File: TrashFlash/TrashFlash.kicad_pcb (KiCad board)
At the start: 2 copper layers, 96 parts, among them IC1 LTC3643IUDD#PBF, IC10 BQ24230RGTR, IC2 ADG5419BCPZ-RL7, IC3 BQ27426YZFR, IC4 SN74LXC2T45QDTTRQ1, IC5 TPS63900DSKR, IC6 TPS63900DSKR, IC7 LP5024RSMR, IC8 AD8615AUJZ-REEL, IC9 BQ29732DSER, J1 USB4800-03-A, Q1 BC56-10PA,115, Q2 BC56-10PA,115, Q3 BC56-10PA,115, Q4 BC56-10PA,115, Q5 PMDPB30XNAX, U1 SI5448DU-T1-GE3, U2 SI5448DU-T1-GE3

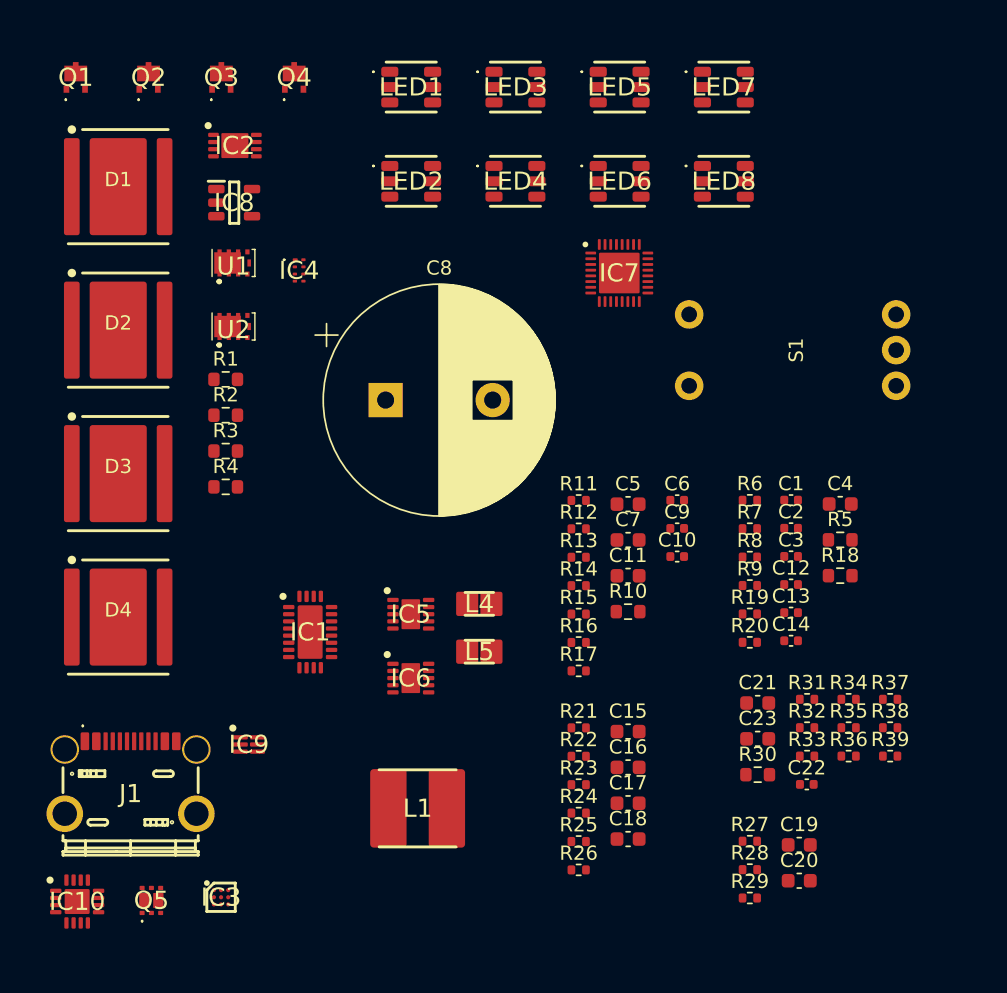
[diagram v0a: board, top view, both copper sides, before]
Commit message: Footprints 3D model fixed
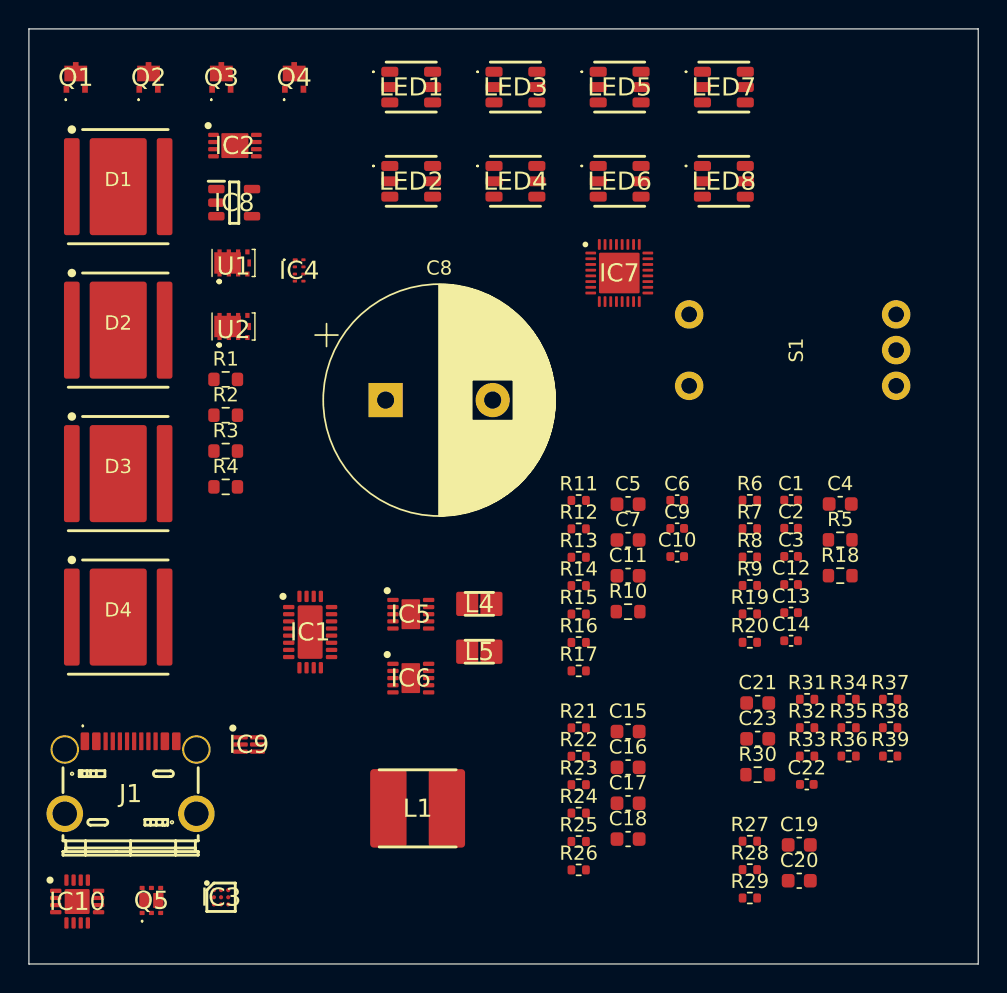
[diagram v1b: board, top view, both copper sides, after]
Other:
- board outline added: 66.5 x 65.5 mm
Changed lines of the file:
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@@
 		)
 		(embedded_fonts no)
-		(model "150353M153300.stp"
+		(model "${KIPRJMOD}/TrashFlash.pretty/3D/150353M153300.stp"
 			(offset
 				(xyz 0 0 0)
@@
 			)
 			(rotate
-				(xyz 0 0 0)
+				(xyz -0 -0 -180)
 			)
 		)
@@
 		)
 		(embedded_fonts no)
-		(model "LP5024RSMR.stp"
+		(model "${KIPRJMOD}/TrashFlash.pretty/3D/LP5024RSMR.stp"
 			(offset
 				(xyz 0 0 0)
@@
 		)
 		(embedded_fonts no)
-		(model "ADG5419BCPZ-RL7.stp"
+		(model "${KIPRJMOD}/TrashFlash.pretty/3D/ADG5419BCPZ-RL7.stp"
 			(offset
 				(xyz 0 0 0)
@@
 		)
 		(embedded_fonts no)
-		(model "PMDPB30XNAX.stp"
+		(model "${KIPRJMOD}/TrashFlash.pretty/3D/PMDPB30XNAX.stp"
 			(offset
-				(xyz 0 0 0.03999999851)
+				(xyz 0 0 0)
 			)
 			(scale
@@
 			)
 			(rotate
-				(xyz 90 -180 0)
+				(xyz 0 0 0)
 			)
 		)
@@
 		)
 		(embedded_fonts no)
-		(model "TPS63900DSKR.stp"
+		(model "${KIPRJMOD}/TrashFlash.pretty/3D/TPS63900DSKR.stp"
 			(offset
 				(xyz 0 0 0)
@@
 		)
 		(embedded_fonts no)
-		(model "${KIPRJMOD}/TrashFlash.pretty/ec11e09244aq.step"
+		(model "${KIPRJMOD}/TrashFlash.pretty/3D/ec11e09244aq.step"
 			(offset
 				(xyz 2.5 7.5 3.5)
@@
 		)
 		(embedded_fonts no)
-		(model "150353M153300.stp"
+		(model "${KIPRJMOD}/TrashFlash.pretty/3D/150353M153300.stp"
 			(offset
 				(xyz 0 0 0)
@@
 			)
 			(rotate
-				(xyz 0 0 0)
+				(xyz -0 -0 -180)
 			)
 		)
@@
 		)
 		(embedded_fonts no)
-		(model "SN74LXC2T45QDTTRQ1.stp"
+		(model "${KIPRJMOD}/TrashFlash.pretty/3D/SN74LXC2T45QDTTRQ1.stp"
 			(offset
 				(xyz 0 0 0)
@@
 			)
 			(rotate
-				(xyz 0 0 0)
+				(xyz -0 -0 -0)
 			)
 		)
@@
 		)
 		(embedded_fonts no)
-		(model "150353M153300.stp"
+		(model "${KIPRJMOD}/TrashFlash.pretty/3D/150353M153300.stp"
 			(offset
 				(xyz 0 0 0)
@@
 			)
 			(rotate
-				(xyz 0 0 0)
+				(xyz -0 -0 -180)
 			)
 		)
@@
 		)
 		(embedded_fonts no)
-		(model "BC56-10PA,115.stp"
+		(model "${KIPRJMOD}/TrashFlash.pretty/3D/BC56-10PA,115.stp"
 			(offset
-				(xyz 0.8600000014 1.509999968 1.129999978)
+				(xyz 0.85 1.55 1.1)
 			)
 			(scale
@@
 			)
 			(rotate
-				(xyz 90 0 -180)
+				(xyz 90 -0 -180)
 			)
 		)
@@
 			)
 		)
+		(model "${KIPRJMOD}/TrashFlash.pretty/3D/SI5448DU-T1-GE3.stp"
+			(offset
+				(xyz 0 0 0)
+			)
+			(scale
+				(xyz 1 1 1)
+			)
+			(rotate
+				(xyz -90 -0 -0)
+			)
+		)
 	)
 	(footprint "TrashFlash:XFL05K"
@@
 		)
 		(embedded_fonts no)
-		(model "TPS63900DSKR.stp"
+		(model "${KIPRJMOD}/TrashFlash.pretty/3D/TPS63900DSKR.stp"
 			(offset
 				(xyz 0 0 0)
@@
 		)
 		(embedded_fonts no)
-		(model "AD8615AUJZ-REEL.stp"
+		(model "${KIPRJMOD}/TrashFlash.pretty/3D/AD8615AUJZ-REEL.stp"
 			(offset
 				(xyz 0 0 0)
@@
 		)
 		(embedded_fonts no)
-		(model "BQ24230RGTR.stp"
+		(model "${KIPRJMOD}/TrashFlash.pretty/3D/BQ24230RGTR.stp"
 			(offset
 				(xyz 0 0 0)
@@
 		)
 		(embedded_fonts no)
-		(model "150353M153300.stp"
+		(model "${KIPRJMOD}/TrashFlash.pretty/3D/150353M153300.stp"
 			(offset
 				(xyz 0 0 0)
@@
 			)
 			(rotate
-				(xyz 0 0 0)
+				(xyz -0 -0 -180)
 			)
 		)
@@
 			)
 		)
+		(model "${KIPRJMOD}/TrashFlash.pretty/3D/SI5448DU-T1-GE3.stp"
+			(offset
+				(xyz 0 0 0)
+			)
+			(scale
+				(xyz 1 1 1)
+			)
+			(rotate
+				(xyz -90 -0 -0)
+			)
+		)
 	)
 	(footprint "Resistor_SMD:R_0402_1005Metric"
@@
 		)
 		(embedded_fonts no)
+		(model "${KIPRJMOD}/TrashFlash.pretty/3D/USB4800-03-A.stp"
+			(offset
+				(xyz 0 -4.25 0)
+			)
+			(scale
+				(xyz 1 1 1)
+			)
+			(rotate
+				(xyz -90 -0 -0)
+			)
+		)
 	)
 	(footprint "Resistor_SMD:R_0402_1005Metric"
@@
 		)
 		(embedded_fonts no)
-		(model "74438343022.stp"
+		(model "${KIPRJMOD}/TrashFlash.pretty/3D/74438343022.stp"
 			(offset
 				(xyz 0 0 0)
@@
 		)
 		(embedded_fonts no)
-		(model "LTC3643IUDD#PBF.stp"
+		(model "${KIPRJMOD}/TrashFlash.pretty/3D/LTC3643IUDD#PBF.stp"
 			(offset
 				(xyz 0 0 0)
@@
 		)
 		(embedded_fonts no)
-		(model "150353M153300.stp"
+		(model "${KIPRJMOD}/TrashFlash.pretty/3D/150353M153300.stp"
 			(offset
 				(xyz 0 0 0)
@@
 			)
 			(rotate
-				(xyz 0 0 0)
+				(xyz -0 -0 -180)
 			)
 		)
@@
 		)
 		(embedded_fonts no)
-		(model "BQ29732DSER.stp"
+		(model "${KIPRJMOD}/TrashFlash.pretty/3D/BQ29732DSER.stp"
 			(offset
-				(xyz 0 0 0.02999999888)
+				(xyz 0 0 0)
 			)
 			(scale
@@
 			)
 			(rotate
-				(xyz -90 0 -90)
+				(xyz -90 -0 -90)
 			)
 		)
@@
 		)
 		(embedded_fonts no)
-		(model "BQ27426YZFR.stp"
+		(model "${KIPRJMOD}/TrashFlash.pretty/3D/BQ27426YZFR.stp"
 			(offset
 				(xyz 0 0 0)
@@
 		)
 		(embedded_fonts no)
-		(model "74438367068.stp"
+		(model "${KIPRJMOD}/TrashFlash.pretty/3D/74438367068.stp"
 			(offset
 				(xyz 0 0 0)
@@
 		)
 		(embedded_fonts no)
-		(model "150353M153300.stp"
+		(model "${KIPRJMOD}/TrashFlash.pretty/3D/150353M153300.stp"
 			(offset
 				(xyz 0 0 0)
@@
 			)
 			(rotate
-				(xyz 0 0 0)
+				(xyz -0 -0 -180)
 			)
 		)
@@
 		)
 		(embedded_fonts no)
-		(model "BC56-10PA,115.stp"
+		(model "${KIPRJMOD}/TrashFlash.pretty/3D/BC56-10PA,115.stp"
 			(offset
-				(xyz 0.8600000014 1.509999968 1.129999978)
+				(xyz 0.85 1.55 1.1)
 			)
 			(scale
@@
 			)
 			(rotate
-				(xyz 90 0 -180)
+				(xyz 90 -0 -180)
 			)
 		)
@@
 		)
 		(embedded_fonts no)
-		(model "BC56-10PA,115.stp"
+		(model "${KIPRJMOD}/TrashFlash.pretty/3D/BC56-10PA,115.stp"
 			(offset
-				(xyz 0.8600000014 1.509999968 1.129999978)
+				(xyz 0.85 1.55 1.1)
 			)
 			(scale
@@
 			)
 			(rotate
-				(xyz 90 0 -180)
+				(xyz 90 -0 -180)
 			)
 		)
@@
 		)
 		(embedded_fonts no)
-		(model "74438343022.stp"
+		(model "${KIPRJMOD}/TrashFlash.pretty/3D/74438343022.stp"
 			(offset
 				(xyz 0 0 0)
@@
 		)
 		(embedded_fonts no)
-		(model "150353M153300.stp"
+		(model "${KIPRJMOD}/TrashFlash.pretty/3D/150353M153300.stp"
 			(offset
 				(xyz 0 0 0)
@@
 			)
 			(rotate
-				(xyz 0 0 0)
+				(xyz -0 -0 -180)
 			)
 		)
@@
 		)
 		(embedded_fonts no)
-		(model "150353M153300.stp"
+		(model "${KIPRJMOD}/TrashFlash.pretty/3D/150353M153300.stp"
 			(offset
 				(xyz 0 0 0)
@@
 			)
 			(rotate
-				(xyz 0 0 0)
+				(xyz -0 -0 -180)
 			)
 		)
@@
 		)
 		(embedded_fonts no)
-		(model "BC56-10PA,115.stp"
+		(model "${KIPRJMOD}/TrashFlash.pretty/3D/BC56-10PA,115.stp"
 			(offset
-				(xyz 0.8600000014 1.509999968 1.129999978)
+				(xyz 0.85 1.55 1.1)
 			)
 			(scale
@@
 			)
 			(rotate
-				(xyz 90 0 -180)
+				(xyz 90 -0 -180)
 			)
 		)
 	)
+	(gr_rect
+		(start 84 71)
+		(end 150.5 136.5)
+		(stroke
+			(width 0.05)
+			(type default)
+		)
+		(fill no)
+		(layer "Edge.Cuts")
+	)
 	(embedded_fonts no)

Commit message: 3d models and footprints
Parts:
- moved C8 50.0 mm to (156.5, 112.5)

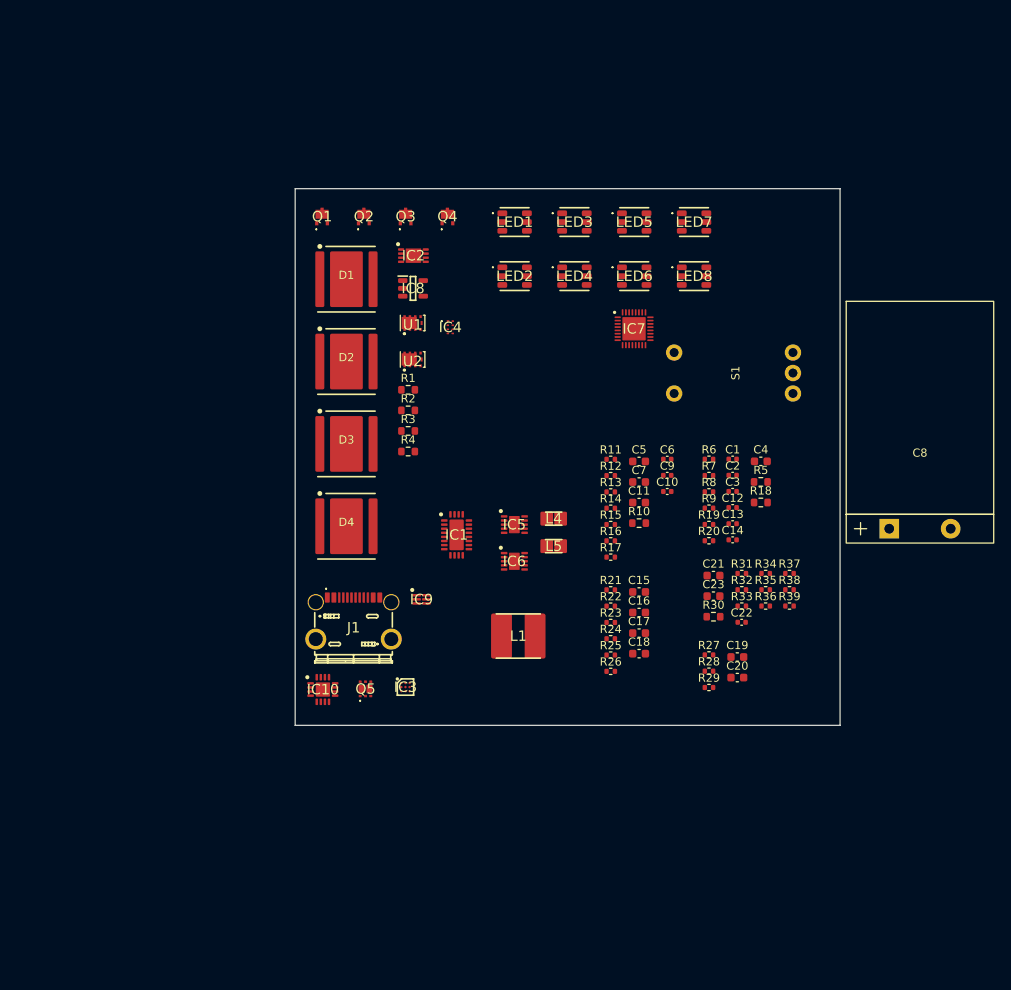
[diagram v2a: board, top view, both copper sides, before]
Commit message: Added 3D-models to footprints, PCB outline and component placement
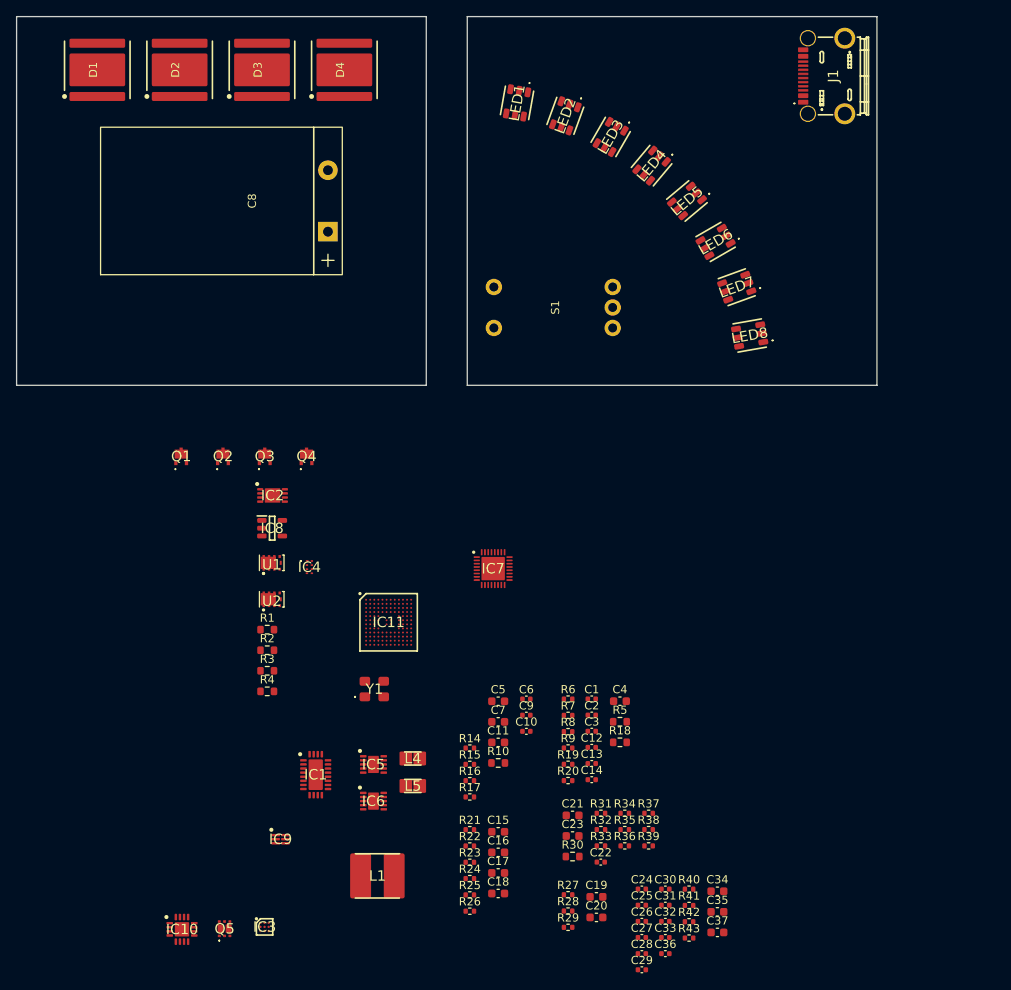
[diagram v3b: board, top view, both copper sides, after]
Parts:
- removed R11: 100k, Resistor_SMD:R_0402_1005Metric
- removed R12: 33k, Resistor_SMD:R_0402_1005Metric
- removed R13: 27k, Resistor_SMD:R_0402_1005Metric
- added C24: 6.8p, Capacitor_SMD:C_0402_1005Metric, F.Cu at (126.3, 156.5)
- added C25: 6.8p, Capacitor_SMD:C_0402_1005Metric, F.Cu at (126.3, 158.4)
- added C26: 100n, Capacitor_SMD:C_0402_1005Metric, F.Cu at (126.3, 160.4)
- added C27: 100n, Capacitor_SMD:C_0402_1005Metric, F.Cu at (126.3, 162.4)
- added C28: 100n, Capacitor_SMD:C_0402_1005Metric, F.Cu at (126.3, 164.4)
- added C29: 100n, Capacitor_SMD:C_0402_1005Metric, F.Cu at (126.3, 166.3)
- added C30: 100n, Capacitor_SMD:C_0402_1005Metric, F.Cu at (129.2, 156.5)
- added C31: 100n, Capacitor_SMD:C_0402_1005Metric, F.Cu at (129.2, 158.4)
- added C32: 100n, Capacitor_SMD:C_0402_1005Metric, F.Cu at (129.2, 160.4)
- added C33: 100n, Capacitor_SMD:C_0402_1005Metric, F.Cu at (129.2, 162.4)
- added C34: 4.7u, Capacitor_SMD:C_0603_1608Metric, F.Cu at (135.5, 156.8)
- added C35: 1u, Capacitor_SMD:C_0603_1608Metric, F.Cu at (135.5, 159.3)
- added C36: 10n, Capacitor_SMD:C_0402_1005Metric, F.Cu at (129.2, 164.4)
- added C37: 1u, Capacitor_SMD:C_0603_1608Metric, F.Cu at (135.5, 161.8)
- added IC11: STM32L471QEI6, TrashFlash:BGA132C50P12X12_700X700X60, F.Cu at (95.4, 123.9)
- added R40: 1k, Resistor_SMD:R_0402_1005Metric, F.Cu at (132.1, 156.5)
- added R41: 1k, Resistor_SMD:R_0402_1005Metric, F.Cu at (132.1, 158.5)
- added R42: 1k, Resistor_SMD:R_0402_1005Metric, F.Cu at (132.1, 160.5)
- added R43: 1k, Resistor_SMD:R_0402_1005Metric, F.Cu at (132.1, 162.5)
- added Y1: ECS-160-8-33B2-CTN-TR3, TrashFlash:ECS160833B2CTNTR3, F.Cu at (93.7, 132.1)
- moved J1 89.2 mm to (149.7, 57.2), turned to 90 degrees
- moved C8 77.5 mm to (88.0, 76.2), turned to 90 degrees
- moved D4 55.7 mm to (90.0, 56.5), turned to 90 degrees
- moved D3 46.8 mm to (80.0, 56.5), turned to 90 degrees
- moved D2 41.0 mm to (69.9, 56.5), turned to 90 degrees
- moved D1 39.7 mm to (59.9, 56.5), turned to 90 degrees
- moved C19 33.9 mm to (120.8, 157.4)
- moved C20 33.9 mm to (120.8, 159.9)
- moved C21 33.9 mm to (117.9, 147.5)
- moved C4 33.9 mm to (123.6, 133.6)
- moved IC1 33.9 mm to (86.5, 142.5)
- moved IC7 33.9 mm to (108.2, 117.4)
- moved L1 33.9 mm to (94.0, 154.9)
- moved R14 33.9 mm to (105.3, 139.3)
- moved R17 33.9 mm to (105.3, 145.2)
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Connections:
- net /LED_Current_Source/EN_0.2A_PATH renamed /LED_Current_Source/EN_LED_RANGE_200mA
- net /LED_Current_Source/EN_20A_PATH renamed /LED_Current_Source/EN_LED_RANGE_20A
- net /LED_Current_Source/SW_IN renamed /LED_Current_Source/SELECT_LED_RANGE
- net /LED_Current_Source/V_CURRENT_SET renamed /LED_Current_Source/VSET_LED_CURRENT
- net /LED_Supply/CAPGD renamed /LED_Supply/LED_DRIVE_CAPACITOR_CHARGED
- net /LED_Supply/PFO renamed /LED_Supply/~{LED_DRIVE_INPUT_POWER_FAIL}
- net /LED_Supply/V_VOLTAGE_SET renamed /LED_Supply/VSET_LED_DRIVE_VOLTAGE
- net /Supply/EN_REG_5V renamed /Supply/EN_5V_REG
- net /Supply/SEL_VDD renamed /Supply/SELECT_VDD
- net Net-(D1-K) renamed /LED_Current_Source/TCA_COLLECTOR
- net Net-(IC10-BAT_1) renamed /Battery_Management/BAT_CHARGER_INOUT
- net Net-(IC10-ISET) renamed /Battery_Management/ISET_CHG
- net Net-(IC10-TMR) renamed /Battery_Management/TMR_CHG
- net Net-(IC10-TS) renamed /Battery_Management/TS_CHG
- net Net-(IC1A-BOOST) renamed /LED_Supply/BOOST_DRV
- net Net-(IC1A-FBCAP) renamed /LED_Supply/FBCAP
- net Net-(IC1A-INDIS_1) renamed /LED_Supply/INDIS_DRV
- net Net-(IC1A-SW_1) renamed /LED_Supply/SW_DRV
- net Net-(IC1A-VIN_1) renamed /LED_Supply/VIN_DRV
- net Net-(IC1B-ILIM) renamed /LED_Supply/ILIM_DRV
- net Net-(IC2-D) renamed /LED_Current_Source/TCA_CURRENT_FB
- net Net-(IC2-SA) renamed /LED_Current_Source/TCA_FB_200mA
- net Net-(IC2-SB) renamed /LED_Current_Source/TCA_FB_20A
- net Net-(IC4-B1) renamed /LED_Current_Source/GATE_DRV_20A
- net Net-(IC5-CFG1) renamed /Supply/CFG1_VDD
- net Net-(IC5-CFG2) renamed /Supply/CFG2_VDD
- net Net-(IC5-CFG3) renamed /Supply/CFG3_VDD
- net Net-(IC5-LX1) renamed /Supply/LX1_VDD
- net Net-(IC5-LX2) renamed /Supply/LX2_VDD
- net Net-(IC6-CFG1) renamed /Supply/CFG1_5V
- net Net-(IC6-CFG2) renamed /Supply/CFG2_5V
- net Net-(IC6-CFG3) renamed /Supply/CFG3_5V
- net Net-(IC6-LX1) renamed /Supply/LX1_5V
- net Net-(IC6-LX2) renamed /Supply/LX2_5V
- net Net-(IC7-IREF) renamed /User_Interface/IREF_RGB
- net Net-(IC7-VCAP) renamed /User_Interface/VCAP_RGB
- net Net-(IC8A-+) renamed /LED_Current_Source/TCA_POS_IN
- net Net-(IC8A--) renamed /LED_Current_Source/TCA_NEG_IN
- net Net-(IC9-BAT) renamed /Battery_Management/VCC_PROT
- net Net-(IC9-COUT) renamed /Battery_Management/COUT
- net Net-(IC9-DOUT) renamed /Battery_Management/DOUT
- net Net-(IC9-V-) renamed /Battery_Management/V-_PROT
- net Net-(J1-CC1) renamed /Battery_Management/CC1
- net Net-(J1-CC2) renamed /Battery_Management/CC2
- net Net-(Q1-B) renamed /LED_Current_Source/TCA_BASE_DRIVE
- net Net-(R1-Pad2) renamed /LED_Current_Source/TCA_EMITTER
- IC1 pad 7: Net-(IC1A-RUN) -> /LED_Supply/EN_LED_DRIVE_BOOST
- IC1 pad 8: Net-(IC1A-FBSYS) -> VSYS
- IC2 pad 5: /LED_Current_Source/SW_EN -> VDD
- IC4 pad 6: Net-(IC4-B2) -> /LED_Current_Source/GATE_DRV_200mA
- IC7 pad 1: Net-(IC7-OUT0) -> /User_Interface/RED0
- IC7 pad 10: Net-(IC7-OUT9) -> /User_Interface/RED3
- IC7 pad 11: Net-(IC7-OUT10) -> /User_Interface/GREEN3
- IC7 pad 12: Net-(IC7-OUT11) -> /User_Interface/BLUE3
- IC7 pad 13: Net-(IC7-OUT12) -> /User_Interface/RED4
- IC7 pad 14: Net-(IC7-OUT13) -> /User_Interface/GREEN4
- IC7 pad 15: Net-(IC7-OUT14) -> /User_Interface/BLUE4
- IC7 pad 16: Net-(IC7-OUT15) -> /User_Interface/RED5
- IC7 pad 17: Net-(IC7-OUT16) -> /User_Interface/GREEN5
- IC7 pad 18: Net-(IC7-OUT17) -> /User_Interface/BLUE5
- IC7 pad 19: Net-(IC7-OUT18) -> /User_Interface/RED6
- IC7 pad 2: Net-(IC7-OUT1) -> /User_Interface/GREEN0
- IC7 pad 20: Net-(IC7-OUT19) -> /User_Interface/GREEN6
- IC7 pad 21: Net-(IC7-OUT20) -> /User_Interface/BLUE6
- IC7 pad 22: Net-(IC7-OUT21) -> /User_Interface/RED7
- IC7 pad 23: Net-(IC7-OUT22) -> /User_Interface/GREEN7
- IC7 pad 24: Net-(IC7-OUT23) -> /User_Interface/BLUE7
- IC7 pad 3: Net-(IC7-OUT2) -> /User_Interface/BLUE0
- IC7 pad 4: Net-(IC7-OUT3) -> /User_Interface/RED1
- IC7 pad 5: Net-(IC7-OUT4) -> /User_Interface/GREEN1
- IC7 pad 6: Net-(IC7-OUT5) -> /User_Interface/BLUE1
- IC7 pad 7: Net-(IC7-OUT6) -> /User_Interface/RED2
- IC7 pad 8: Net-(IC7-OUT7) -> /User_Interface/GREEN2
- IC7 pad 9: Net-(IC7-OUT8) -> /User_Interface/BLUE2
- LED1 pad 2: Net-(IC7-OUT0) -> /User_Interface/RED0
- LED1 pad 4: Net-(IC7-OUT1) -> /User_Interface/GREEN0
- LED1 pad 6: Net-(IC7-OUT2) -> /User_Interface/BLUE0
- LED2 pad 2: Net-(IC7-OUT6) -> /User_Interface/RED0
- LED2 pad 4: Net-(IC7-OUT7) -> /User_Interface/GREEN0
- LED2 pad 6: Net-(IC7-OUT8) -> /User_Interface/BLUE0
- LED3 pad 2: Net-(IC7-OUT3) -> /User_Interface/RED0
- LED3 pad 4: Net-(IC7-OUT4) -> /User_Interface/GREEN0
- LED3 pad 6: Net-(IC7-OUT5) -> /User_Interface/BLUE0
- LED4 pad 2: Net-(IC7-OUT9) -> /User_Interface/RED0
- LED4 pad 4: Net-(IC7-OUT10) -> /User_Interface/GREEN0
- LED4 pad 6: Net-(IC7-OUT11) -> /User_Interface/BLUE0
- LED5 pad 2: Net-(IC7-OUT12) -> /User_Interface/RED0
- LED5 pad 4: Net-(IC7-OUT13) -> /User_Interface/GREEN0
- LED5 pad 6: Net-(IC7-OUT14) -> /User_Interface/BLUE0
- LED6 pad 2: Net-(IC7-OUT15) -> /User_Interface/RED0
- LED6 pad 4: Net-(IC7-OUT16) -> /User_Interface/GREEN0
- LED6 pad 6: Net-(IC7-OUT17) -> /User_Interface/BLUE0
- LED7 pad 2: Net-(IC7-OUT18) -> /User_Interface/RED0
- LED7 pad 4: Net-(IC7-OUT19) -> /User_Interface/GREEN0
- LED7 pad 6: Net-(IC7-OUT20) -> /User_Interface/BLUE0
- LED8 pad 2: Net-(IC7-OUT21) -> /User_Interface/RED0
- LED8 pad 4: Net-(IC7-OUT22) -> /User_Interface/GREEN0
- LED8 pad 6: Net-(IC7-OUT23) -> /User_Interface/BLUE0
- R19 pad 1: Net-(IC4-B2) -> /LED_Current_Source/GATE_DRV_200mA
- R19 pad 2: Net-(IC4-B2) -> Net-(R19-Pad2)
- U1 pad 3: Net-(IC4-B2) -> Net-(R19-Pad2)
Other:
- board size 66.5 x 65.5 mm -> 105 x 45 mm
